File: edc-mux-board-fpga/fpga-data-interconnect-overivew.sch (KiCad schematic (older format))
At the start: 0 parts

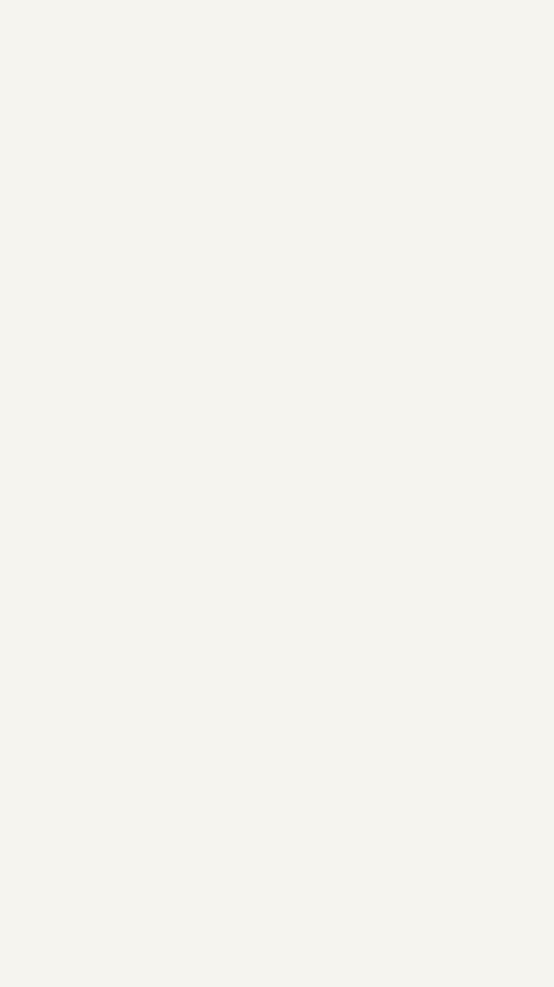
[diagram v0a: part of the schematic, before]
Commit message: moved 1:8 clock buffers from clock sheet to reduce amount of intersheet wiring at top levels
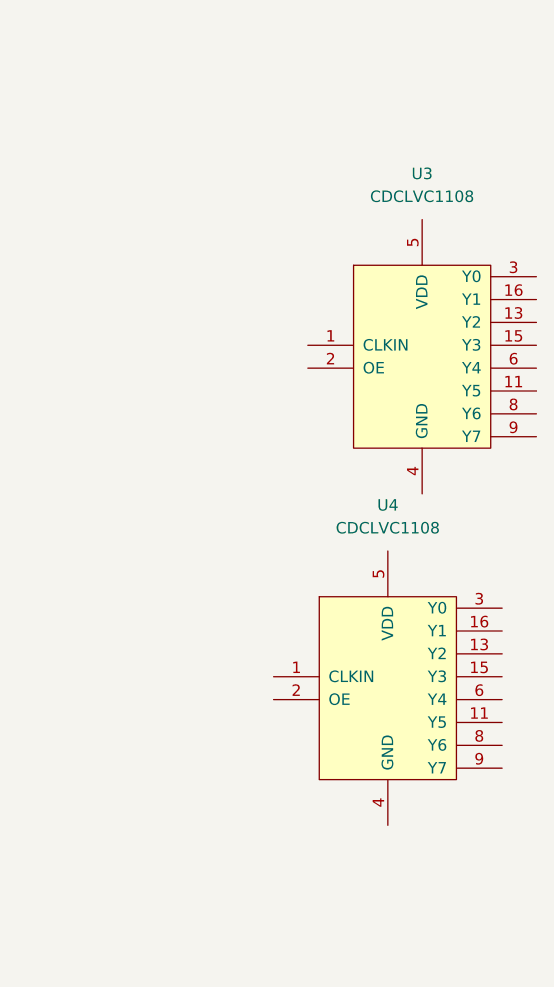
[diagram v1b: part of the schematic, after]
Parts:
- added U3, U4: CDCLVC1108, Package_SO:TSSOP-16_4.4x5mm_P0.65mm, symbol SW-Texas:CDCLVC1108
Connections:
- new net: U3.10 (VDD), U3.14 (VDD), U3.5 (VDD)
- new net: U3.12 (GND), U3.4 (GND), U3.7 (GND)
- new net: U4.10 (VDD), U4.14 (VDD), U4.5 (VDD)
- new net: U4.12 (GND), U4.4 (GND), U4.7 (GND)
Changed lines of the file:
@@
 F1 "conn16.sch" 50
 $EndSheet
+$Comp
+L SW-Texas:CDCLVC1108 U?
+U 1 1 5CB315C0
+P 5500 5000
+AR Path="/5CB315C0" Ref="U?"  Part="1"
+AR Path="/5CC3E5DC/5CB315C0" Ref="U?"  Part="1"
+AR Path="/5CC6CC1A/5CB315C0" Ref="U3"  Part="1"
+F 0 "U3" H 5500 5800 50  0000 C CNN
+F 1 "CDCLVC1108" H 5500 5700 50  0000 C CNN
+F 2 "Package_SO:TSSOP-16_4.4x5mm_P0.65mm" H 5700 5800 50  0001 C CNN
+F 3 "https://www.ti.com/lit/ds/symlink/cdclvc1108.pdf" H 5450 6100 50  0001 C CNN
+	1    5500 5000
+	1    0    0    -1
+$EndComp
+$Comp
+L SW-Texas:CDCLVC1108 U?
+U 1 1 5CB315C6
+P 5350 6450
+AR Path="/5CB315C6" Ref="U?"  Part="1"
+AR Path="/5CC3E5DC/5CB315C6" Ref="U?"  Part="1"
+AR Path="/5CC6CC1A/5CB315C6" Ref="U4"  Part="1"
+F 0 "U4" H 5350 7250 50  0000 C CNN
+F 1 "CDCLVC1108" H 5350 7150 50  0000 C CNN
+F 2 "Package_SO:TSSOP-16_4.4x5mm_P0.65mm" H 5550 7250 50  0001 C CNN
+F 3 "https://www.ti.com/lit/ds/symlink/cdclvc1108.pdf" H 5300 7550 50  0001 C CNN
+	1    5350 6450
+	1    0    0    -1
+$EndComp
 $EndSCHEMATC

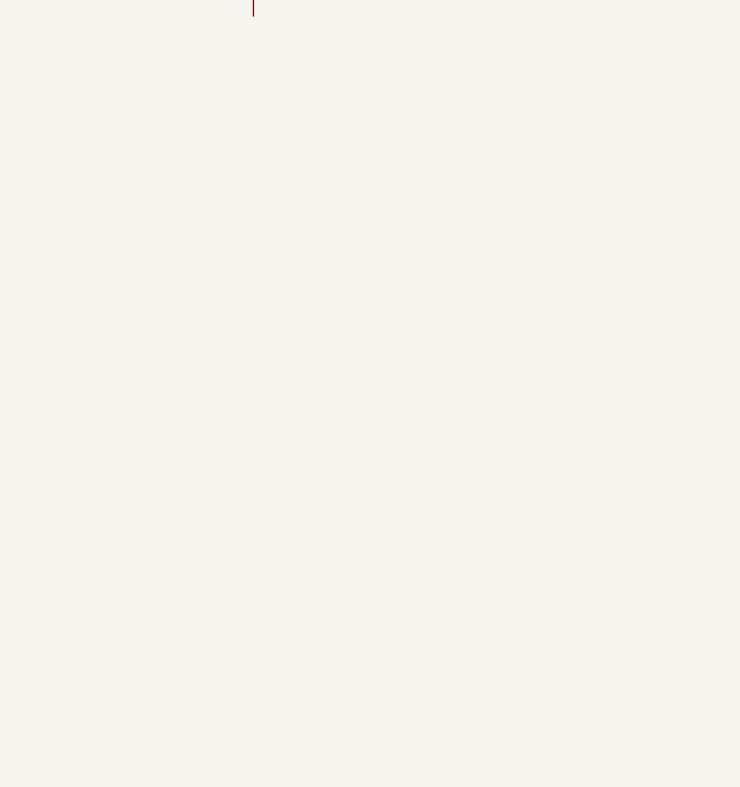
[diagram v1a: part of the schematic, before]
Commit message: added 2 i2c muxes
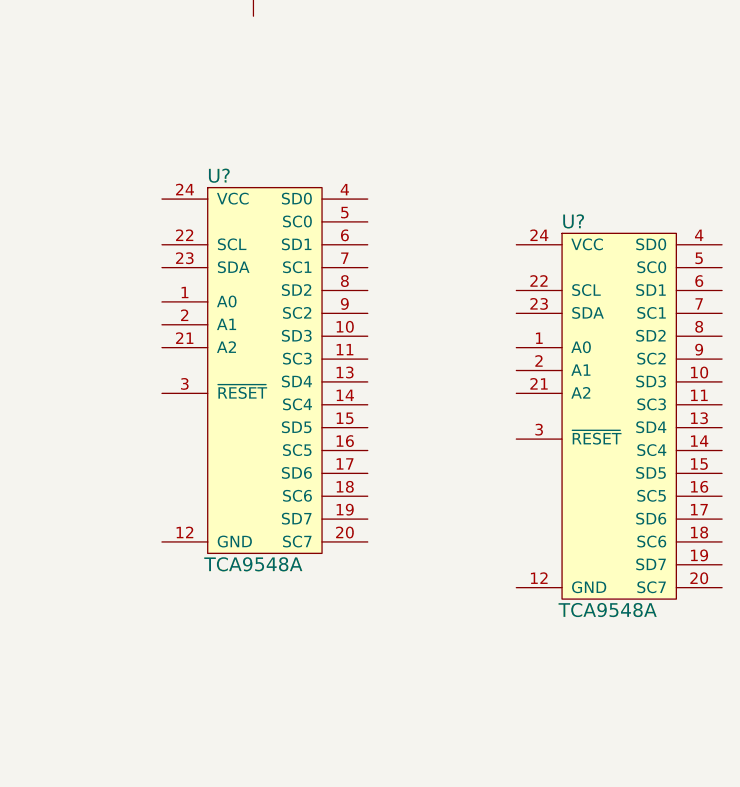
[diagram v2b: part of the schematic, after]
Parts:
- added U? (x2): TCA9548A, Housings_SSOP:TSSOP-24_4.4x7.8mm_Pitch0.65mm, symbol SW-Texas:TCA9548A
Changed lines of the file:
@@
+	1    0    0    -1
+$EndComp
+$Comp
+L SW-Texas:TCA9548A U?
+U 1 1 5CDE50BB
+P 5400 8600
+F 0 "U?" H 5200 9450 60  0000 C CNN
+F 1 "TCA9548A" H 5350 7750 60  0000 C CNN
+F 2 "Housings_SSOP:TSSOP-24_4.4x7.8mm_Pitch0.65mm" H 5550 10300 60  0001 C CNN
+F 3 "http://www.ti.com/lit/ds/symlink/tca9548a.pdf" H 5500 10400 60  0001 C CNN
+F 4 "Texas Instruments" H 5450 10500 60  0001 C CNN "Manufacturer"
+F 5 "Low-Voltage 8-Channel I2C Switch with Reset" H 5550 10600 60  0001 C CNN "Description"
+F 6 "TSSOP24" H 5650 10700 60  0001 C CNN "Package ID"
+F 7 "0.00@0" H 5500 10800 60  0001 C CNN "Pricing"
+	1    5400 8600
+	1    0    0    -1
+$EndComp
+$Comp
+L SW-Texas:TCA9548A U?
+U 1 1 5CDE5FBD
+P 6950 8800
+F 0 "U?" H 6750 9650 60  0000 C CNN
+F 1 "TCA9548A" H 6900 7950 60  0000 C CNN
+F 2 "Housings_SSOP:TSSOP-24_4.4x7.8mm_Pitch0.65mm" H 7100 10500 60  0001 C CNN
+F 3 "http://www.ti.com/lit/ds/symlink/tca9548a.pdf" H 7050 10600 60  0001 C CNN
+F 4 "Texas Instruments" H 7000 10700 60  0001 C CNN "Manufacturer"
+F 5 "Low-Voltage 8-Channel I2C Switch with Reset" H 7100 10800 60  0001 C CNN "Description"
+F 6 "TSSOP24" H 7200 10900 60  0001 C CNN "Package ID"
+F 7 "0.00@0" H 7050 11000 60  0001 C CNN "Pricing"
+	1    6950 8800
 	1    0    0    -1
 $EndComp
